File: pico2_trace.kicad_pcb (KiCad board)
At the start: 2 copper layers, 92 x 64 mm, 56 parts, among them J1B BREAKOUT, J2B BREAKOUT, J3 MIPI-20, J4 JST-SH-3 DEBUG, J5 USB-A HOST, J6 CORTEX-10, J7 JST-SH-3 DEBUG_PROBE, J8 USB-MICROB PWR, J9 USB-MICROB DEV, SW1 RESET

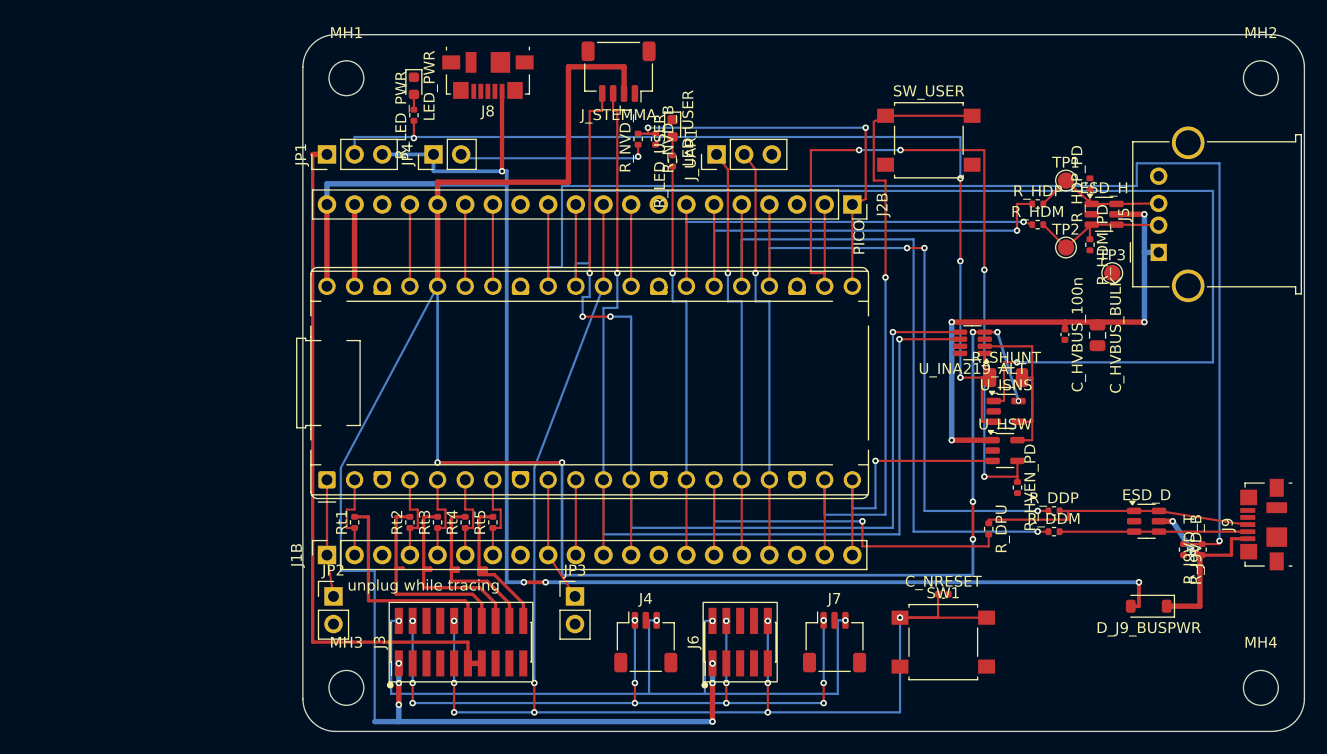
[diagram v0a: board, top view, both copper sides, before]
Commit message: lib: SMT footprints incl. 5905-style Pico socket (THT elimination)
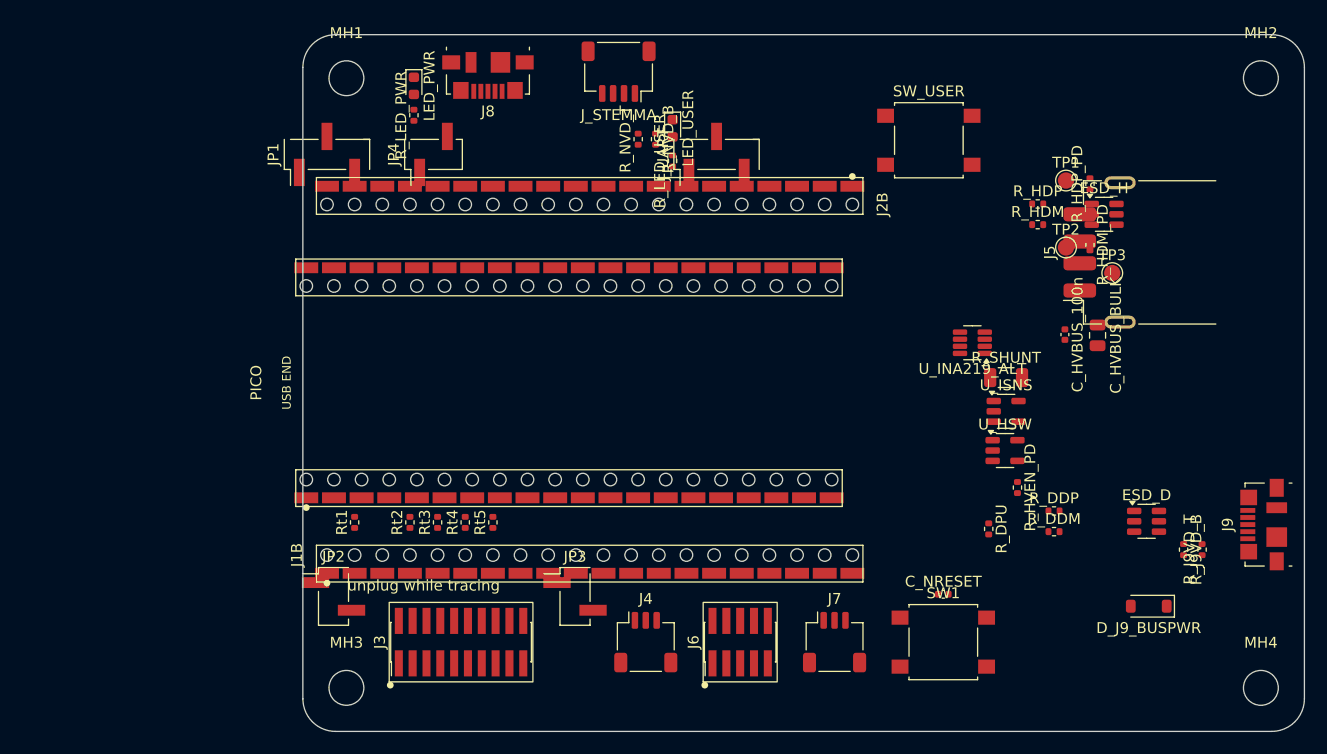
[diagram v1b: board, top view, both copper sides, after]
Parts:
- removed the J1B at (2.21, 47.8)
- removed the J2B at (50.5, 15.6)
- removed the J_UART at (38.0, 11.0)
- removed the PICO at (2.21, 40.9)
- added J1B: BREAKOUT, PinSocket_1x20_SMD_ThruHole, F.Cu at (2.21, 47.8)
- added J2B: BREAKOUT, PinSocket_1x20_SMD_ThruHole, F.Cu at (50.5, 15.6)
- added J_UART: UART0, PinHeader_1x03_P2.54mm_Vertical_SMD_Pin1Left, F.Cu at (38.0, 11.0)
- added PICO: Pico2, PicoSocket_2x20_SMD_ThruHole, F.Cu at (0.31, 40.9)
- J5: footprint USB_A_Molex_67643_Horizontal -> USB_A_Receptacle_GCT_USB1046
- JP1: footprint PinHeader_1x03_P2.54mm_Vertical -> PinHeader_1x03_P2.54mm_Vertical_SMD_Pin1Left
- JP2, JP3, JP4: footprint PinHeader_1x02_P2.54mm_Vertical -> PinHeader_1x02_P2.54mm_Vertical_SMD_Pin1Left
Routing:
- net P3V3: track 233.0 -> 0.00 mm, vias 13 -> 0
- net VBUS_NET: track 145.4 -> 0.00 mm, vias 4 -> 0
- net NRESET: track 127.9 -> 0.00 mm, vias 9 -> 0
- net DEV_VBUS_DET: track 120.4 -> 0.00 mm, vias 1 -> 0
- net ISENSE: track 114.2 -> 0.00 mm, vias 1 -> 0
- net I2C0_SCL: track 101.2 -> 0.00 mm, vias 4 -> 0
- net I2C0_SDA: track 99.7 -> 0.00 mm, vias 2 -> 0
- net VBUS_SEL: track 92.0 -> 0.00 mm, vias 4 -> 0
- net HOST_VBUS_EN: track 72.2 -> 0.00 mm, vias 4 -> 0
- net SWDIO: track 70.7 -> 0.00 mm, vias 4 -> 0
- net SWCLK: track 68.1 -> 0.00 mm, vias 12 -> 0
- net GP19: track 66.8 -> 0.00 mm, vias 1 -> 0
- net V5_JTRACE: track 63.6 -> 0.00 mm
- net BTN_USER: track 62.0 -> 0.00 mm, vias 1 -> 0
- net GP18: track 60.8 -> 0.00 mm, vias 3 -> 0
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
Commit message: lib: blind-bottom SMT sockets (stock land pattern, no through-holes)
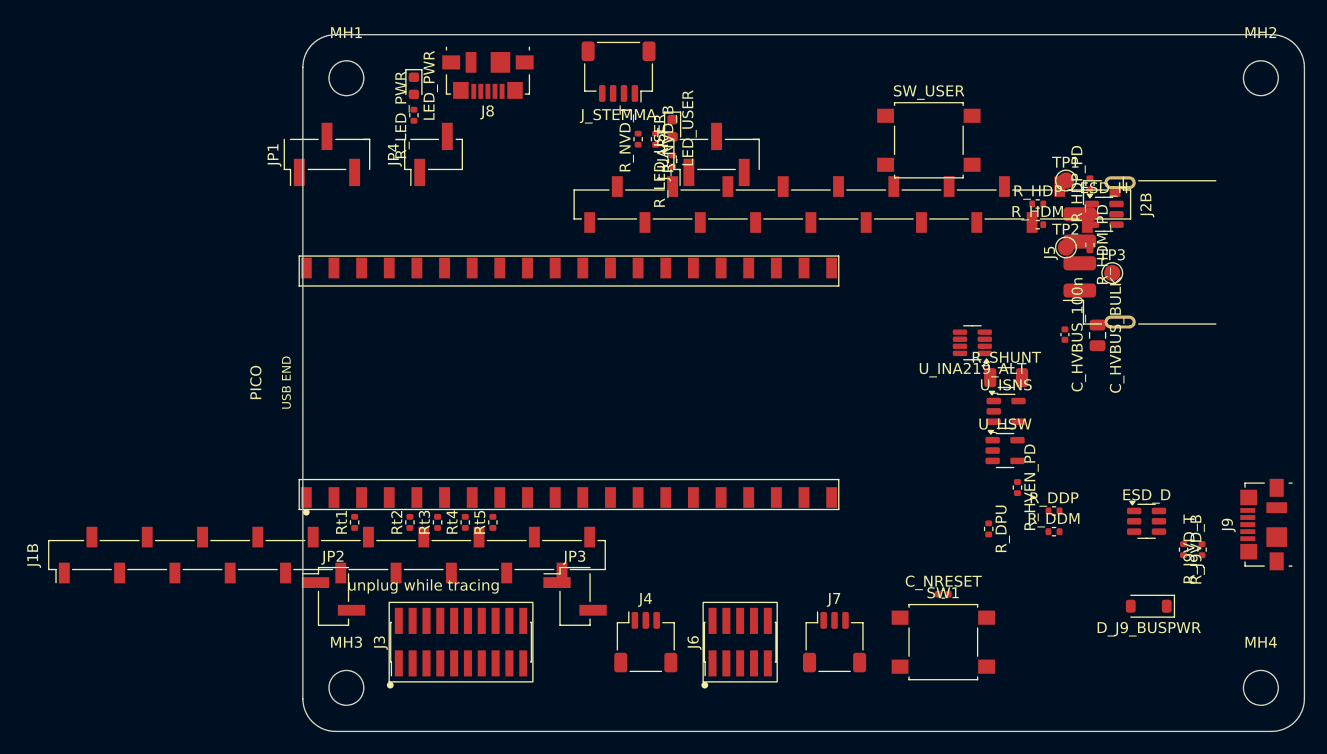
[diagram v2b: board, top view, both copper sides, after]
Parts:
- removed the J1B at (2.21, 47.8)
- removed the J2B at (50.5, 15.6)
- removed the PICO at (0.31, 40.9)
- added J1B: BREAKOUT, PinSocket_1x20_P2.54mm_Vertical_SMD_Pin1Left, F.Cu at (2.21, 47.8)
- added J2B: BREAKOUT, PinSocket_1x20_P2.54mm_Vertical_SMD_Pin1Left, F.Cu at (50.5, 15.6)
- added PICO: Pico2, PicoSocket_2x20_SMD, F.Cu at (0.31, 40.9)

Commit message: pcb: re-place for SMT footprints + silkscreen polish
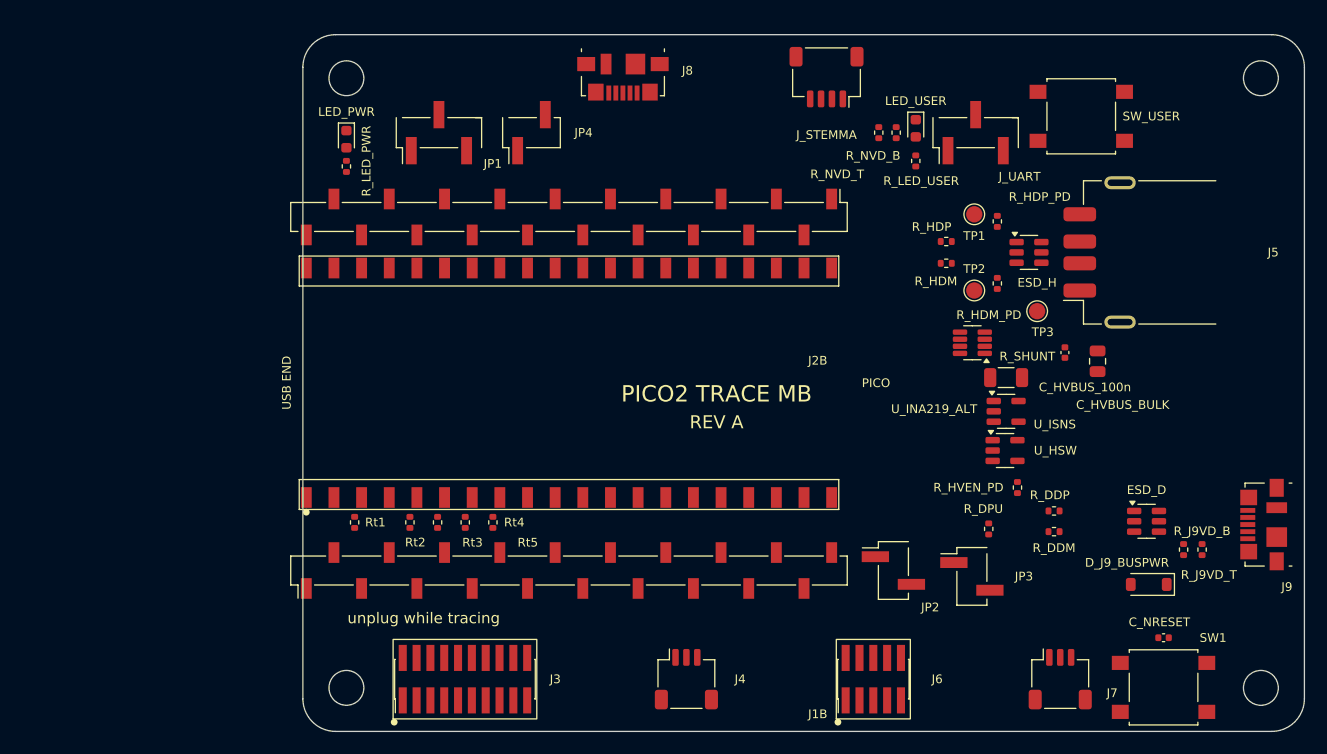
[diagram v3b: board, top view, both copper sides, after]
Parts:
- moved JP2 51.5 mm to (54.2, 49.2)
- moved JP3 36.5 mm to (61.5, 49.8)
- moved J2B 26.1 mm to (24.4, 16.7)
- moved J_UART 23.9 mm to (61.8, 9.00)
- moved LED_USER 22.3 mm to (56.3, 8.60)
- moved R_LED_USER 22.3 mm to (56.3, 11.6)
- moved J1B 22.3 mm to (24.4, 49.2)
- moved R_NVD_B 22.1 mm to (54.5, 9.00)
- moved R_NVD_T 22.1 mm to (52.9, 9.00)
- moved J7 21.0 mm to (69.6, 59.2)
- moved SW1 20.7 mm to (79.1, 60.0)
- moved C_NRESET 20.6 mm to (79.1, 55.4)
- moved J_STEMMA 19.1 mm to (48.1, 3.90)
- moved SW_USER 14.2 mm to (71.5, 7.50)
- moved J6 12.7 mm to (52.4, 59.2)
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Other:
- board text added: "PICO2 TRACE MB"
- board text added: "REV A"

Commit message: pcb: revert hand-inserted connectors to THT, re-place, relocate guards
Parts that take repeated hand-insertion force stay through-hole; everything
else stays SMT. Reverts pico_socket/breakout_1x20/hdr_1x02/hdr_1x03/hdr_1x06
to stock THT footprints, retires the custom SMD Pico-socket land pattern
(never itself a traced, orderable part -- the project's largest remaining
fab risk), and re-places J1B/J2B/JP1-4/J_UART against the reverted
footprints' pin-1 anchors. JP2/JP3 (GP0/GP6 guard jumpers) move back into
the J1B->debug-row gap, now that THT J1B's courtyard is slim enough to fit
them -- guard-trace runs to PICO shrink from 42-50mm to ~11.4mm each.

Rt1-5, the debug row, and every cluster outside PICO's own footprint are
unchanged (not PICO-grid-dependent). Breakout pad alignment verified exact
(0.000mm error, all 40 J1B/J2B<->PICO pairs) by construction: both parts
share PICO's 2.54mm pitch and pad-1-first numbering.

Regenerated pico2_trace.net/.kicad_sch/docs/schematic.pdf (embedded
footprint names); netlists match, ERC 0 errors. DRC: 2 pre-existing
silk_edge_clearance violations only (PICO's own edge overhang, a Task 11
decision), courtyards_overlap/holes_co_located/silk_overlap/silk_over_copper
all 0. No routing performed (placement only).
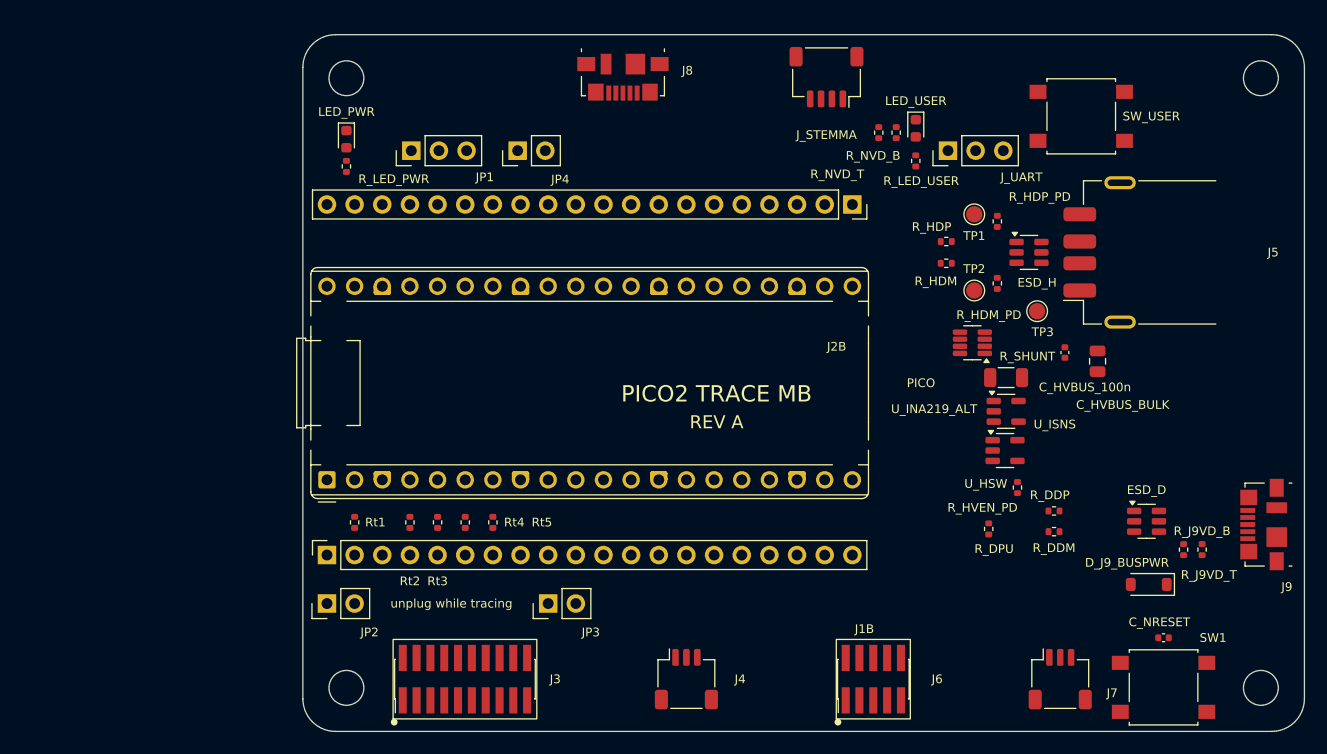
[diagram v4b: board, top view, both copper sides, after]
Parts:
- removed the J1B at (24.4, 49.2)
- removed the J2B at (24.4, 16.7)
- removed the J_UART at (61.8, 9.00)
- removed the PICO at (0.31, 40.9)
- added J1B: BREAKOUT, PinSocket_1x20_P2.54mm_Vertical, F.Cu at (2.21, 47.8)
- added J2B: BREAKOUT, PinSocket_1x20_P2.54mm_Vertical, F.Cu at (50.5, 15.6)
- added J_UART: UART0, PinHeader_1x03_P2.54mm_Vertical, F.Cu at (59.3, 10.7)
- added PICO: Pico2, RaspberryPi_Pico_Common_THT, F.Cu at (2.21, 40.9)
- JP1: footprint PinHeader_1x03_P2.54mm_Vertical_SMD_Pin1Left -> PinHeader_1x03_P2.54mm_Vertical
- JP2, JP3, JP4: footprint PinHeader_1x02_P2.54mm_Vertical_SMD_Pin1Left -> PinHeader_1x02_P2.54mm_Vertical
- moved JP2 52.1 mm to (2.21, 52.3), turned to 90 degrees
- moved JP3 39.0 mm to (22.5, 52.3), turned to 90 degrees
- moved JP1 3.03 mm to (9.96, 10.7)
- moved JP4 2.09 mm to (19.7, 10.7)

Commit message: pcb: route all copper (0 non-GND unconnected)
Routes the trace bundle (TRACECLK/TD0-3 + GP1-5), guard nets (GP0/GP6),
the SWD/NRESET/P3V3(VTref) tree, all 40 breakout stubs, and SW1/SW_USER
internal pad ties -- DRC-clean (0 clearance/shorting/crossing/hole
violations, only the 2 pre-existing silk_edge_clearance warnings from
PICO's intentional edge overhang).

Re-placement (Task 14e) invalidated the prior router's coordinates:
J3/J6 pads are 2.4mm tall not wide (footprint rotation swaps W/H), the
board is 92.1x64.1mm (too short for the old "stack 4 B_Cu trunks south
of SW1" strategy), and MH3's courtyard now overlaps the old P3V3 descent
column. Redesigned the SWD tree so SWDIO+NRESET share the tight 1.5mm
inter-row gap as B_Cu (NRESET hops over SWDIO), while SWCLK+P3V3 use
F_Cu for their entire run instead -- different-layer copper needs no
mutual clearance, which is what makes 4 nets fit a gap that can't hold
more than 2 same-layer occupants.

The remaining ~65 non-GND pad-pairs (power tree, USB legs, dividers,
misc GPIO) were attempted but not brought to a clean state given an
undocumented "Antenna Copper Keep Out" zone on PICO's own footprint
(x=43.345-52.345, y=24.9-39.1) plus routing density from ~14 nets
sharing the same narrow row-crossing corridors -- left unrouted rather
than commit crossings/shorts. Exact pairs and a recommended approach
are in .superpowers/sdd/task-14f-report.md (gitignored, local only).
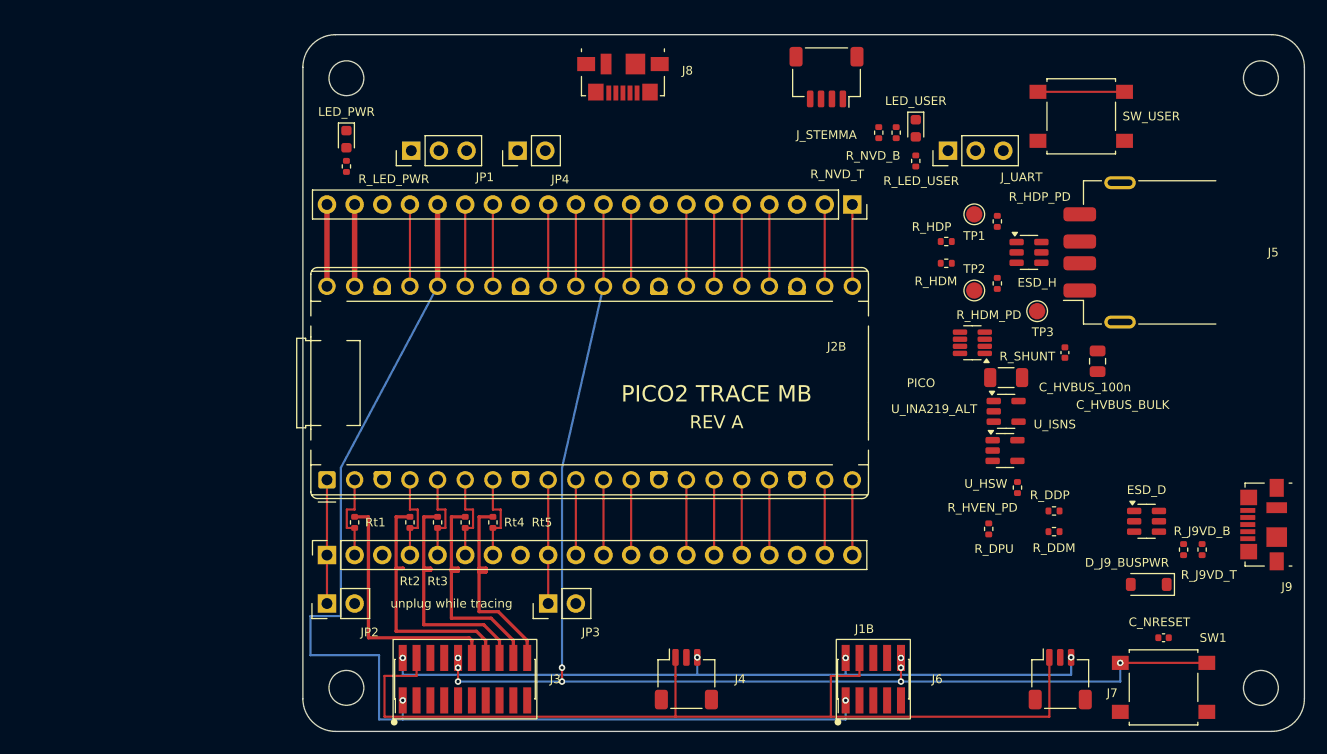
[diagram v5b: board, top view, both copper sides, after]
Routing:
- net NRESET: track 0.00 -> 119.1 mm, vias 0 -> 9
- net P3V3: track 0.00 -> 105.0 mm, vias 0 -> 2
- net SWCLK: track 0.00 -> 88.3 mm
- net SWDIO: track 0.00 -> 67.7 mm, vias 0 -> 4
- net TD1: track 0.00 -> 24.2 mm
- net TD2: track 0.00 -> 23.8 mm
- net TRACECLK: track 0.00 -> 23.6 mm
- net TD3: track 0.00 -> 23.4 mm
- net TD0: track 0.00 -> 23.2 mm
- net BTN_USER: track 0.00 -> 14.9 mm
- net GP6: track 0.00 -> 11.4 mm
- net GP0: track 0.00 -> 11.4 mm
- net GP4: track 0.00 -> 8.35 mm
- net GP3: track 0.00 -> 8.35 mm
- net GP1: track 0.00 -> 8.35 mm
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
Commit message: pcb: add J10 SWD dupont, clear antenna keepout, complete routing
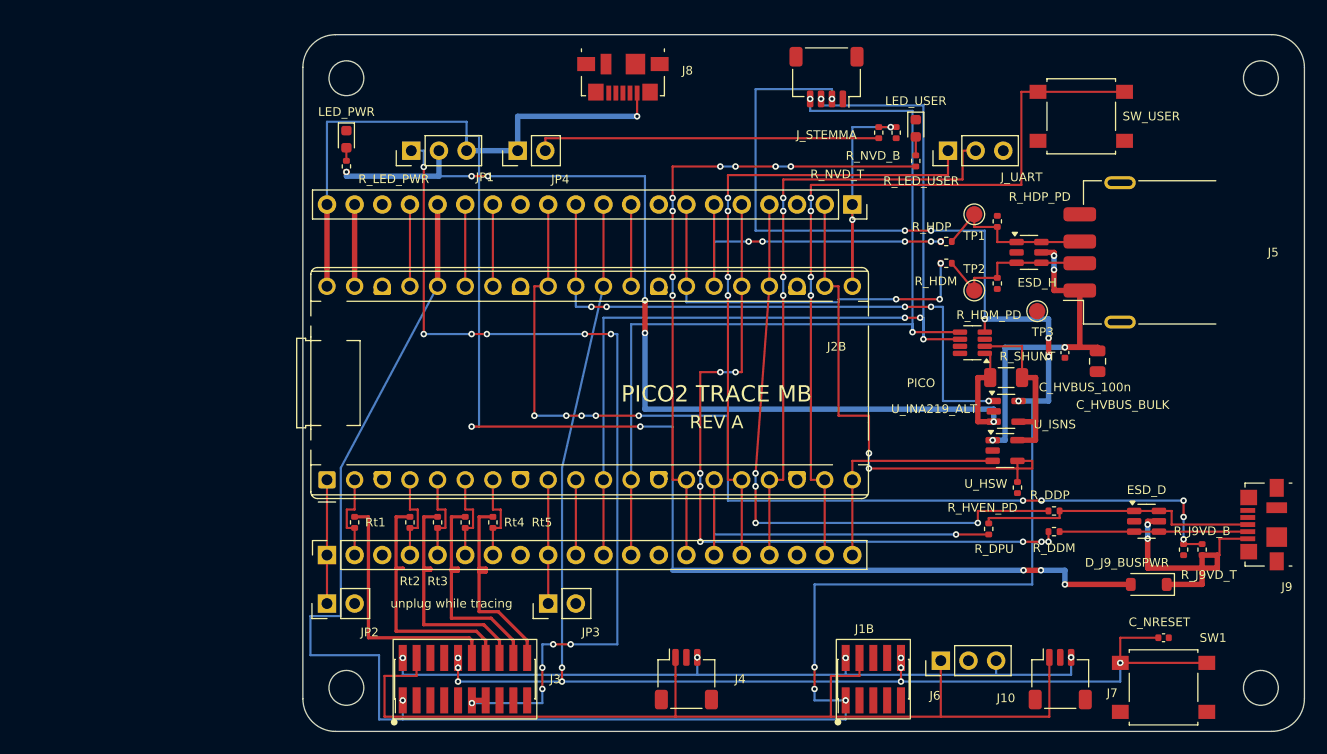
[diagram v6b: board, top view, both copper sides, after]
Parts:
- added J10: SWD, PinHeader_1x03_P2.54mm_Vertical, F.Cu at (58.6, 57.5)
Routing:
- net VBUS_NET: track 7.51 -> 164.0 mm, vias 0 -> 6
- net P3V3: track 105.0 -> 224.0 mm, vias 2 -> 11
- net VBUS_SEL: track 0.00 -> 94.1 mm, vias 0 -> 6
- net DEV_VBUS_DET: track 7.51 -> 93.8 mm, vias 0 -> 10
- net V5_JTRACE: track 0.00 -> 84.5 mm, vias 0 -> 11
- net I2C0_SDA: track 6.91 -> 88.0 mm, vias 0 -> 4
- net I2C0_SCL: track 6.91 -> 83.0 mm, vias 0 -> 2
- net GP19: track 7.51 -> 67.7 mm, vias 0 -> 8
- net BTN_USER: track 14.9 -> 72.6 mm, vias 0 -> 4
- net GP10: track 6.91 -> 59.3 mm, vias 0 -> 8
- net UART0_TX: track 6.91 -> 58.6 mm, vias 0 -> 4
- net GP18: track 7.51 -> 57.3 mm, vias 0 -> 4
- net UART0_RX: track 6.91 -> 56.1 mm, vias 0 -> 4
- net ISENSE: track 7.51 -> 56.4 mm, vias 0 -> 5
- net HOST_VBUS_EN: track 7.51 -> 47.3 mm, vias 0 -> 2
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
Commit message: pcb: remove redundant J4, widen power traces off the pitch crossings
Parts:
- removed J4: JST-SH-3 DEBUG, JST_SH_SM03B-SRSS-TB_1x03-1MP_P1.00mm_Horizontal
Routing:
- net SWCLK: track 93.5 -> 88.0 mm
- net SWDIO: track 69.0 -> 67.4 mm, vias 4 -> 3
